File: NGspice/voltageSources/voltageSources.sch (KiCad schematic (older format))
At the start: 12 parts

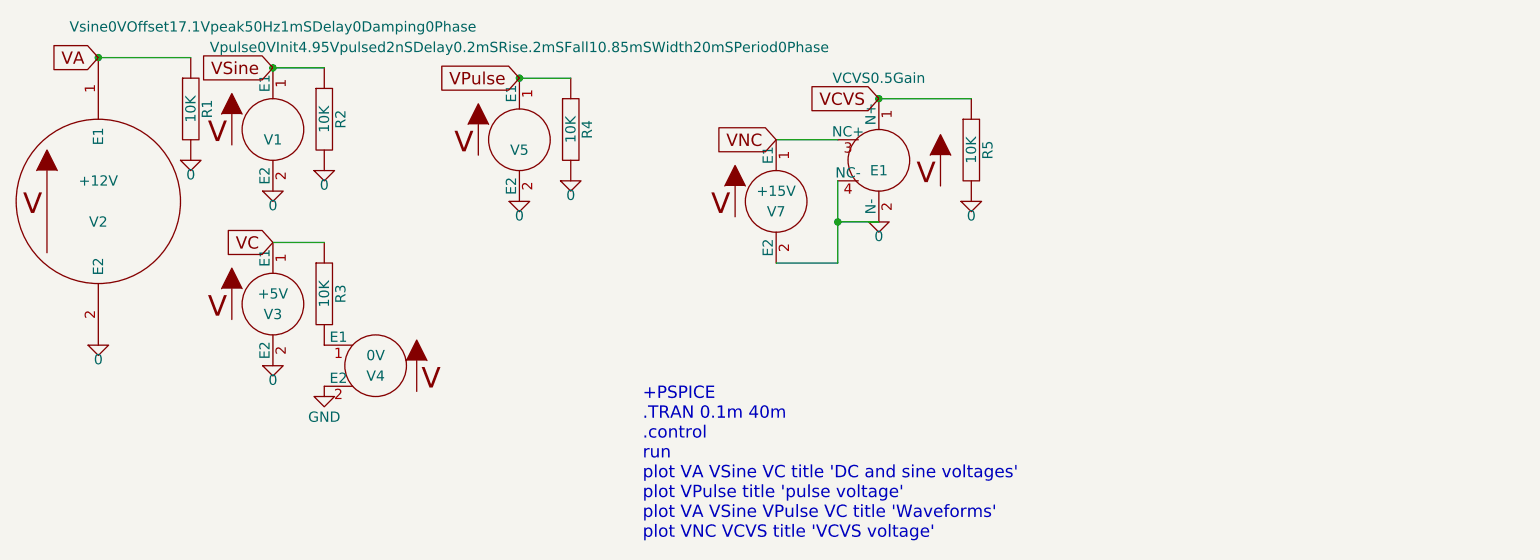
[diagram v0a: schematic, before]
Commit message: added Non-linear voltage source with equation
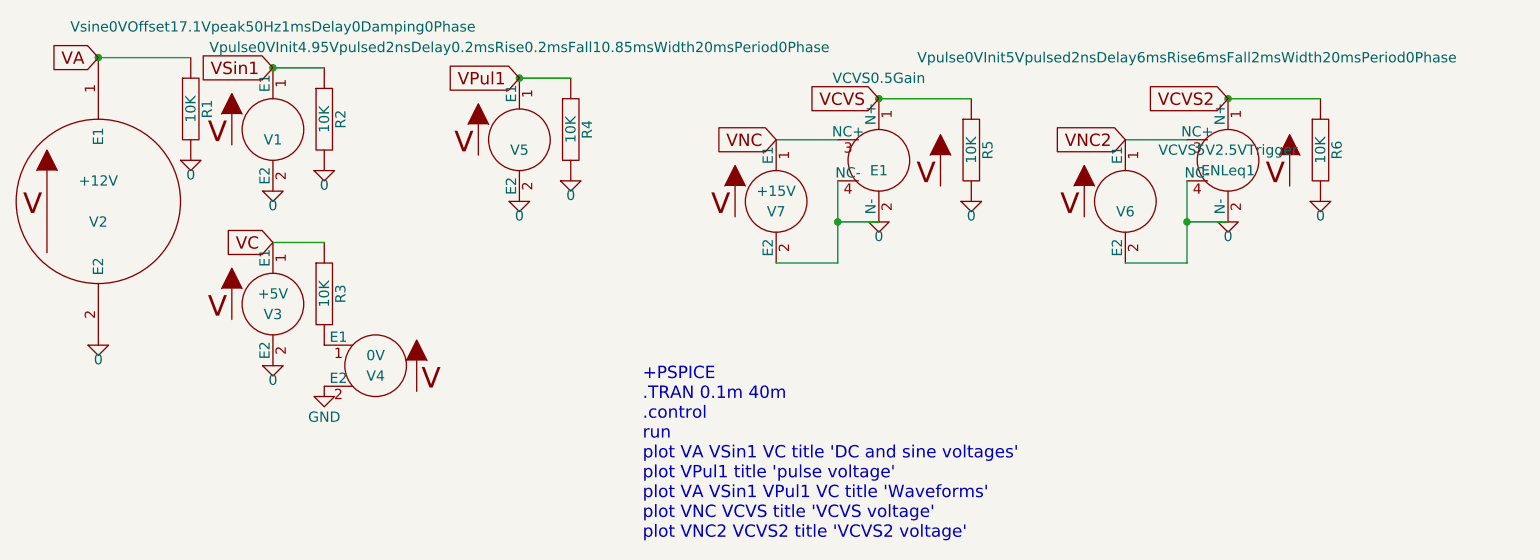
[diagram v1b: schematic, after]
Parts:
- added ENLeq1: VCVS5V2.5VTrigger, symbol VCVS5V2.5VTrigger
- added R6: 10K, symbol R
- added V6: Vpulse0VInit5Vpulsed2nsDelay6msRise6msFall2msWidt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, symbol Vpulse0VInit5Vpulsed2nsDelay2msRise2msFall8msWidth20msPeriod0Phase
- V1: value Vsine0VOffset17.1Vpeak50Hz1mSDelay0Damping0Phase -> Vsine0VOffset17.1Vpeak50Hz1msDelay0Damping0Phase
- V5: value Vpulse0VInit4.95Vpulsed2nSDelay0.2mSRise.2mSFall10.85mSWidth20mSPeriod0Phase -> Vpulse0VInit4.95Vpulsed2nsDelay0.2msRise0.2msFall10.85msWidth20msPeriod0Phase
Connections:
- net 0: now also ENLeq1.2 (N-), ENLeq1.4 (NC-), R6.2, V6.2 (E2)
- net VPulse renamed VPul1
- net VSine renamed VSin1
- new net VCVS2: ENLeq1.1 (N+), R6.1
- new net VNC2: ENLeq1.3 (NC+), V6.1 (E1)
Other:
- note added: "+PSPICE\n.TRAN 0.1m 40m\n.control\nrun\nplot VA VSin1 VC title 'DC and sine voltages'\nplot VPul1 title 'pulse voltage'\nplot VA VSin1 VPul1 VC title 'Waveforms'\nplot VNC VCVS title 'VCVS voltage'\nplot VNC2 VCVS2 title 'VCVS2 voltage'\n"
- note removed: "+PSPICE\n.TRAN 0.1m 40m\n.control\nrun\nplot VA VSine VC title 'DC and sine voltages'\nplot VPulse title 'pulse voltage'\nplot VA VSine VPulse VC title 'Waveforms'\nplot VNC VCVS title 'VCVS voltage'\n"
